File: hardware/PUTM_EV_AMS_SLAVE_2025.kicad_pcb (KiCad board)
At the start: 4 copper layers, 100 x 20 mm, 138 parts, among them CN7 4x100nF, IC2 BQ79616PAPR, J2 B02B-PASK-1, J3 B02B-PASK-1, J4 IDC24, Q2 100V/2W

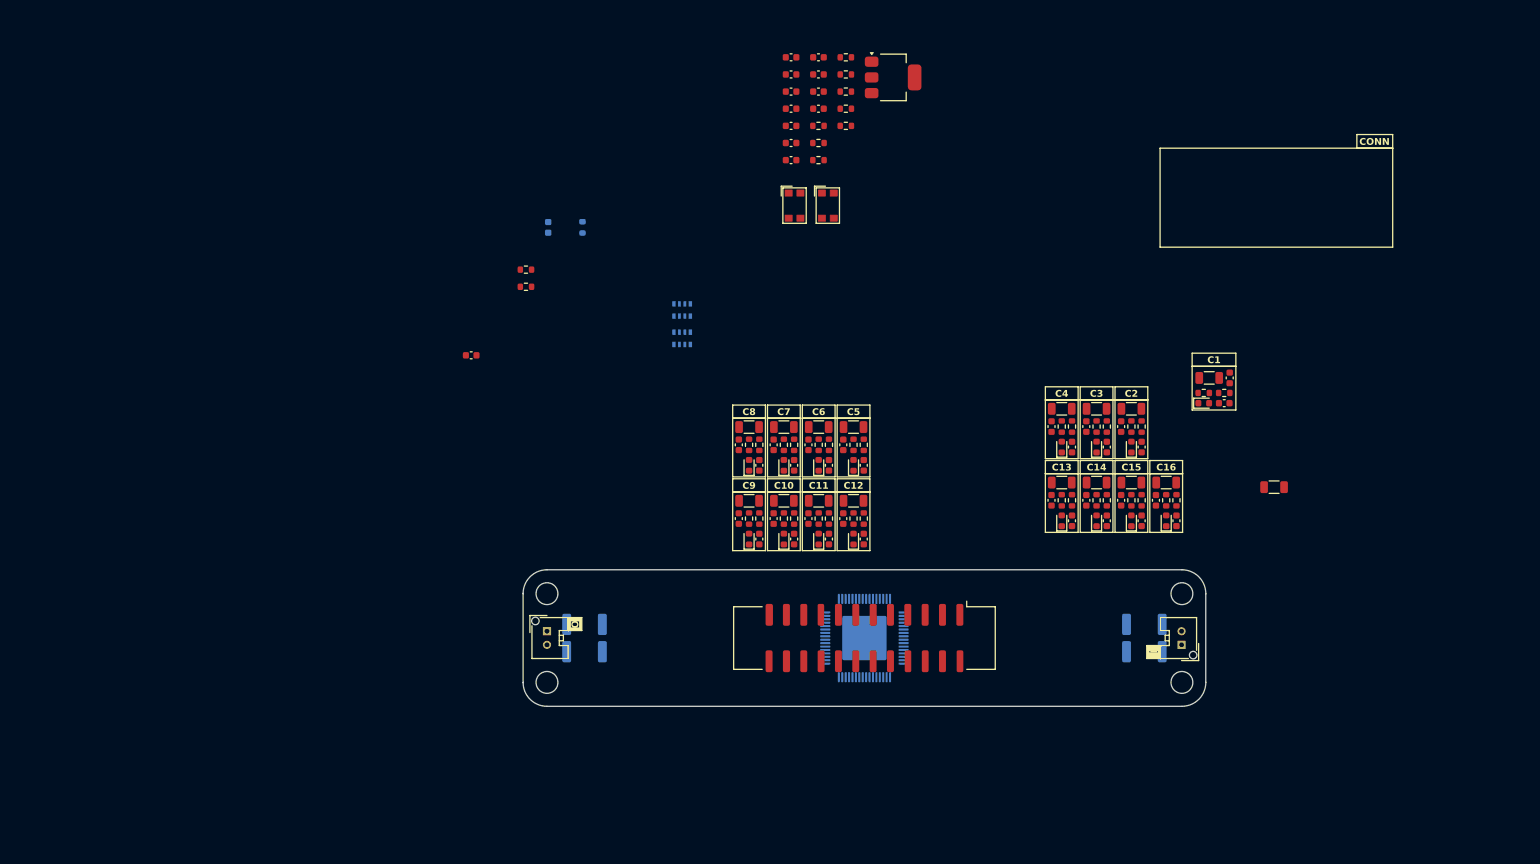
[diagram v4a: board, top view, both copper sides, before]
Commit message: changed back harwin connectors, COM first fitting
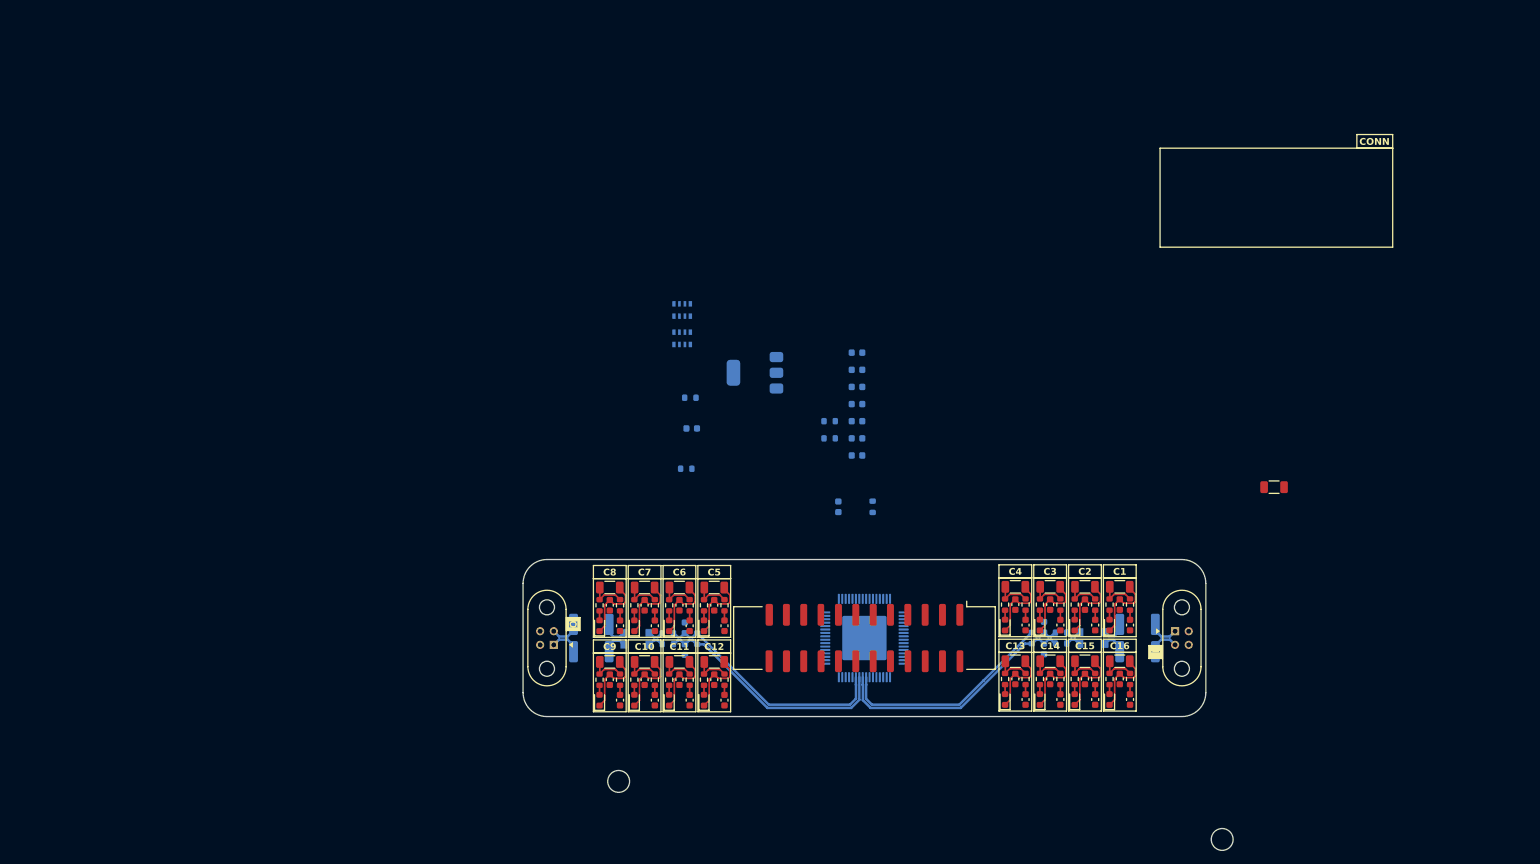
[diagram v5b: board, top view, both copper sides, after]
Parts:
- removed J3: B02B-PASK-1, Samacsys:B02BPASK1LFSN
- removed the REF** at (196.5, 113.5)
- removed the REF** at (103.5, 126.5)
- added J1: M80-5100405, Samacsys:M80-51004YY, F.Cu at (103.5, 120.0)
- C38, C39, C40, C41, C42, C43, C44, C45, C46, C47, C48, C49, L1, L2, Q2, R50, R52, R53, R54, R55, R56, R57, R58, R59, R60: moved to B.Cu
- J2: value B02B-PASK-1 -> M80-5100405; footprint Samacsys:B02BPASK1LFSN -> Samacsys:M80-51004YY
- moved J2 93.0 mm to (196.5, 120.0), turned to -90 degrees
- moved C47 90.4 mm to (176.3, 121.6), turned to -90 degrees
- moved C46 89.8 mm to (176.3, 118.4), turned to 90 degrees
- moved R56 88.3 mm to (121.2, 119.3)
- moved R57 87.4 mm to (121.2, 120.9), turned to 180 degrees
- moved R58 84.5 mm to (174.5, 120.0), turned to -90 degrees
- moved C48 84.0 mm to (123.7, 121.7), turned to -90 degrees
- moved R59 83.0 mm to (178.8, 119.2), turned to 180 degrees
- moved R60 82.1 mm to (178.8, 120.8)
- moved C49 78.5 mm to (123.7, 118.5), turned to 90 degrees
- moved L1 76.9 mm to (183.4, 120.0), turned to 90 degrees
- moved R55 72.3 mm to (125.5, 120.1), turned to 90 degrees
- moved L2 69.4 mm to (116.6, 120.1), turned to 90 degrees
- moved C4 59.0 mm to (146.2, 100.8)
- moved R2 59.0 mm to (151.2, 100.8)
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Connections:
- net /TH7+ renamed /AUX/TH7+
- net Net-(IC2-AVDD) renamed /BQ79616/AVDD
- net Net-(IC2-BAT) renamed /BQ79616/BAT
- net Net-(IC2-COMHN) renamed /BQ79616/IC_COMHN
- net Net-(IC2-COMHP) renamed /BQ79616/IC_COMHP
- net Net-(IC2-CVDD) renamed /BQ79616/CVDD
- net Net-(IC2-DVDD) renamed /BQ79616/DVDD
- net Net-(IC2-LDOIN) renamed /BQ79616/LDOIN
- net Net-(IC2-NEG5V) renamed /BQ79616/NEG5V
- net Net-(IC2-NPNB) renamed /BQ79616/NPNB
- net Net-(IC2-REFHP) renamed /BQ79616/REFHM
- net Net-(Q2-C) renamed /BQ79616/NPNC
- C46 pad 1: Net-(IC2-COMLN) -> /BQ79616/IC_COMLP
- C47 pad 1: Net-(IC2-COMLP) -> /BQ79616/IC_COMLN
- C5 pad 1: /IB+ -> /OL+
- C6 pad 1: /IB- -> /OL-
- C7 pad 1: /IN+ -> /IN-
- C7 pad 2: /IA+ -> /IL-
- C8 pad 1: /IN- -> /IN+
- C8 pad 2: /IA- -> /IL+
- IC2 pad 40: Net-(IC2-COMLP) -> /BQ79616/IC_COMLP
- IC2 pad 41: Net-(IC2-COMLN) -> /BQ79616/IC_COMLN
- J2 pad 1: Net-(J2-Pin_1) -> /IN+
- J2 pad 2: Net-(J2-Pin_2) -> /IN-
- L1 pad 1: Net-(J3-Pin_1) -> /IL-
- L1 pad 2: /IN+ -> /I-
- L1 pad 3: /IN- -> /I+
- L1 pad 4: Net-(J3-Pin_2) -> /IL+
- L2 pad 1: /OUT+ -> /O-
- L2 pad 2: Net-(J2-Pin_1) -> /OL-
- L2 pad 3: Net-(J2-Pin_2) -> /OL+
- L2 pad 4: /OUT- -> /O+
- R2 pad 2: Net-(RN7-R1.2) -> /BQ79616/TSREF
- R56 pad 1: /IB+ -> /O+
- R57 pad 2: /IB- -> /O-
- R58 pad 1: Net-(IC2-COMLN) -> /BQ79616/IC_COMLP
- R58 pad 2: Net-(IC2-COMLP) -> /BQ79616/IC_COMLN
- R59 pad 1: /IA- -> /I+
- R59 pad 2: Net-(IC2-COMLN) -> /BQ79616/IC_COMLP
- R60 pad 1: Net-(IC2-COMLP) -> /BQ79616/IC_COMLN
- R60 pad 2: /IA+ -> /I-
- RN7 pad 5: Net-(RN7-R1.2) -> /BQ79616/TSREF
- RN7 pad 6: Net-(RN7-R1.2) -> /BQ79616/TSREF
- RN7 pad 7: Net-(RN7-R1.2) -> /BQ79616/TSREF
- RN7 pad 8: Net-(RN7-R1.2) -> /BQ79616/TSREF
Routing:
- net /BQ79616/IC_COMLN: track 0.00 -> 36.9 mm
- net /BQ79616/IC_COMLP: track 0.00 -> 36.6 mm
- net /BQ79616/IC_COMHN: track 0.00 -> 35.9 mm
- net /BQ79616/IC_COMHP: track 0.00 -> 35.6 mm
- net /BQ79616/CB5: track 0.00 -> 10.7 mm
- net /BQ79616/CB4: track 0.00 -> 10.7 mm
- net /BQ79616/CB3: track 0.00 -> 10.7 mm
- net /BQ79616/CB12: track 0.00 -> 10.7 mm
- net /BQ79616/CB7: track 0.00 -> 10.7 mm
- net /BQ79616/CB6: track 0.00 -> 10.7 mm
- net /BQ79616/CB8: track 0.00 -> 10.7 mm
- net /BQ79616/CB13: track 0.00 -> 10.7 mm
- net /BQ79616/CB14: track 0.00 -> 10.7 mm
- net /BQ79616/CB10: track 0.00 -> 10.7 mm
- net /BQ79616/CB11: track 0.00 -> 10.7 mm
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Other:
- board size 100 x 20 mm -> 100 x 23 mm

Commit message: sync
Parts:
- moved R51 44.1 mm to (166.8, 106.7)
- moved REF** 30.8 mm to (103.5, 112.0)
- moved REF** 22.2 mm to (196.5, 128.1)
- moved J2 3.80 mm to (196.5, 116.2)
- moved J1 3.70 mm to (103.5, 123.7)
- moved C48 2.70 mm to (126.4, 121.7)
- moved C49 2.70 mm to (126.4, 118.5)
- moved C5 2.70 mm to (112.7, 118.0)
- moved C6 2.70 mm to (112.7, 122.0)
- moved L2 2.70 mm to (119.3, 120.1)
- moved R56 2.70 mm to (123.9, 119.3)
- moved R57 2.70 mm to (123.9, 120.9)
- moved R55 2.70 mm to (128.2, 120.1)
- moved C46 2.60 mm to (173.7, 118.4)
- moved C47 2.60 mm to (173.7, 121.6)
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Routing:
- net /BQ79616/IC_COMLN: track 36.9 -> 0.00 mm
- net /BQ79616/IC_COMLP: track 36.6 -> 0.00 mm
- net /BQ79616/IC_COMHN: track 35.9 -> 0.00 mm
- net /BQ79616/IC_COMHP: track 35.6 -> 0.00 mm
- net /OL+: track 4.80 -> 0.00 mm
- net /OUT-: track 4.47 -> 0.00 mm
- net /OUT+: track 4.47 -> 0.00 mm
- net /IN-: track 4.47 -> 0.00 mm
- net /IN+: track 4.47 -> 0.00 mm
- net /OL-: track 3.64 -> 0.00 mm
- net /IL+: track 3.62 -> 0.00 mm
- net /IL-: track 3.56 -> 0.00 mm
- net /O-: track 2.52 -> 0.00 mm
- net /O+: track 2.52 -> 0.00 mm
- net /I-: track 2.43 -> 0.00 mm
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
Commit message: some visual touch ups, added aux diodes for checking comm with IC, temp meas section, fliped the connector to the other side etc.
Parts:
- removed C4: 100nF, Capacitor_SMD:C_0603_1608Metric
- removed CN7: 4x100nF, Resistor_SMD:R_Array_Convex_4x0603
- added D17: LED, LED_SMD:LED_0603_1608Metric, F.Cu at (153.2, 95.0)
- added D18: LED, LED_SMD:LED_0603_1608Metric, F.Cu at (153.2, 97.5)
- added R61: 510, Resistor_SMD:R_0603_1608Metric, F.Cu at (149.7, 95.0)
- added RN1: 4x10k, Resistor_SMD:R_Array_Convex_4x0603, F.Cu at (163.5, 117.5)
- added TH1: 10k/β=?, Resistor_SMD:R_0603_1608Metric, F.Cu at (149.7, 97.5)
- added TH2: 10k/β=?, Resistor_SMD:R_0603_1608Metric, F.Cu at (149.7, 100.0)
- C38, C40, C41, C42, C43, C44, C45, IC2, Q2, R50, R53, R54, RN7: moved to F.Cu
- C39: value 10nF -> 10nF/100V; moved to F.Cu
- J4: moved to B.Cu
- R2: value 10k -> 510; moved to F.Cu
- R52: value 30 -> 30/100mW; moved to F.Cu
- moved R52 61.4 mm to (184.7, 104.0), turned to 0 degrees
- moved C38 61.3 mm to (184.7, 102.0), turned to 0 degrees
- moved RN7 60.6 mm to (163.5, 121.5), turned to 0 degrees
- moved R53 49.3 mm to (193.3, 98.0), turned to 0 degrees
- moved R54 49.3 mm to (193.3, 100.5), turned to 0 degrees
- moved Q2 45.5 mm to (178.5, 90.5), turned to 0 degrees
- moved C39 41.5 mm to (189.3, 88.0), turned to 0 degrees
- moved R50 34.2 mm to (157.2, 95.0), turned to 0 degrees
- moved C40 13.7 mm to (161.7, 85.5), turned to 0 degrees
- moved C43 13.7 mm to (161.7, 93.0), turned to 0 degrees
- moved C41 13.7 mm to (161.7, 88.0), turned to 0 degrees
- moved C42 13.7 mm to (161.7, 90.5), turned to 0 degrees
- moved C44 13.7 mm to (161.7, 95.5), turned to 0 degrees
- moved C45 13.7 mm to (161.7, 98.1), turned to 0 degrees
- moved R2 9.78 mm to (151.5, 91.0), turned to 0 degrees
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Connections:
- C38 pad 1: /BQ79616/C1- -> /C1-
- C39 pad 2: /BQ79616/C1- -> /C1-
- C40 pad 2: /BQ79616/C1- -> /C1-
- C41 pad 2: /BQ79616/C1- -> /C1-
- C42 pad 2: /BQ79616/C1- -> /C1-
- C43 pad 2: /BQ79616/C1- -> /C1-
- C44 pad 2: /BQ79616/C1- -> /C1-
- C45 pad 2: /BQ79616/C1- -> /C1-
- C46 pad 2: /BQ79616/C1- -> /C1-
- C47 pad 2: /BQ79616/C1- -> /C1-
- C48 pad 2: /BQ79616/C1- -> /C1-
- C49 pad 2: /BQ79616/C1- -> /C1-
- IC2 pad 36: /BQ79616/C1- -> /C1-
- IC2 pad 39: /BQ79616/C1- -> /C1-
- IC2 pad 46: /BQ79616/C1- -> /C1-
- IC2 pad 50: /BQ79616/C1- -> /C1-
- IC2 pad 54: unconnected-(IC2-GPIO8-Pad54) -> /BQ79616/AUX2/TH8+
- IC2 pad 55: unconnected-(IC2-GPIO7-Pad55) -> /AUX/TH7+
- IC2 pad 56: unconnected-(IC2-GPIO6-Pad56) -> /TH6+
- IC2 pad 57: unconnected-(IC2-GPIO5-Pad57) -> /TH5+
- IC2 pad 58: unconnected-(IC2-GPIO4-Pad58) -> /TH4+
- IC2 pad 59: unconnected-(IC2-GPIO3-Pad59) -> /TH3+
- IC2 pad 60: unconnected-(IC2-GPIO2-Pad60) -> /TH2+
- IC2 pad 61: unconnected-(IC2-GPIO1-Pad61) -> /TH1+
- IC2 pad 65: /BQ79616/C1- -> /C1-
- R2 pad 1: /TH1+ -> /BQ79616/CVDD
- R2 pad 2: /BQ79616/TSREF -> Net-(D17-A)
- R50 pad 1: /BQ79616/C1- -> /C1-
- R51 pad 1: /BQ79616/C1- -> /C1-
- R54 pad 1: /BQ79616/C1- -> /C1-
- RN7 pad 1: /TH2+ -> /TH5+
- RN7 pad 2: /TH3+ -> /TH6+
- RN7 pad 3: /TH4+ -> /AUX/TH7+
- RN7 pad 4: /TH5+ -> /BQ79616/AUX2/TH8+
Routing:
- net /OUT-: track 0.00 -> 6.84 mm
- net /OUT+: track 0.00 -> 6.84 mm
- net /IN-: track 0.00 -> 6.54 mm
- net /IN+: track 0.00 -> 6.54 mm
- net /BQ79616/IC_COMHP: track 0.00 -> 4.44 mm
- net /BQ79616/IC_COMHN: track 0.00 -> 4.44 mm
- net /BQ79616/IC_COMLP: track 0.00 -> 4.44 mm
- net /BQ79616/IC_COMLN: track 0.00 -> 4.44 mm
- net /IL-: track 0.00 -> 2.62 mm
- net /IL+: track 0.00 -> 2.62 mm
- net /OL-: track 0.00 -> 2.62 mm
- net /OL+: track 0.00 -> 2.62 mm
- net /O-: track 0.00 -> 2.43 mm
- net /O+: track 0.00 -> 2.43 mm
- net /I-: track 0.00 -> 2.43 mm
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
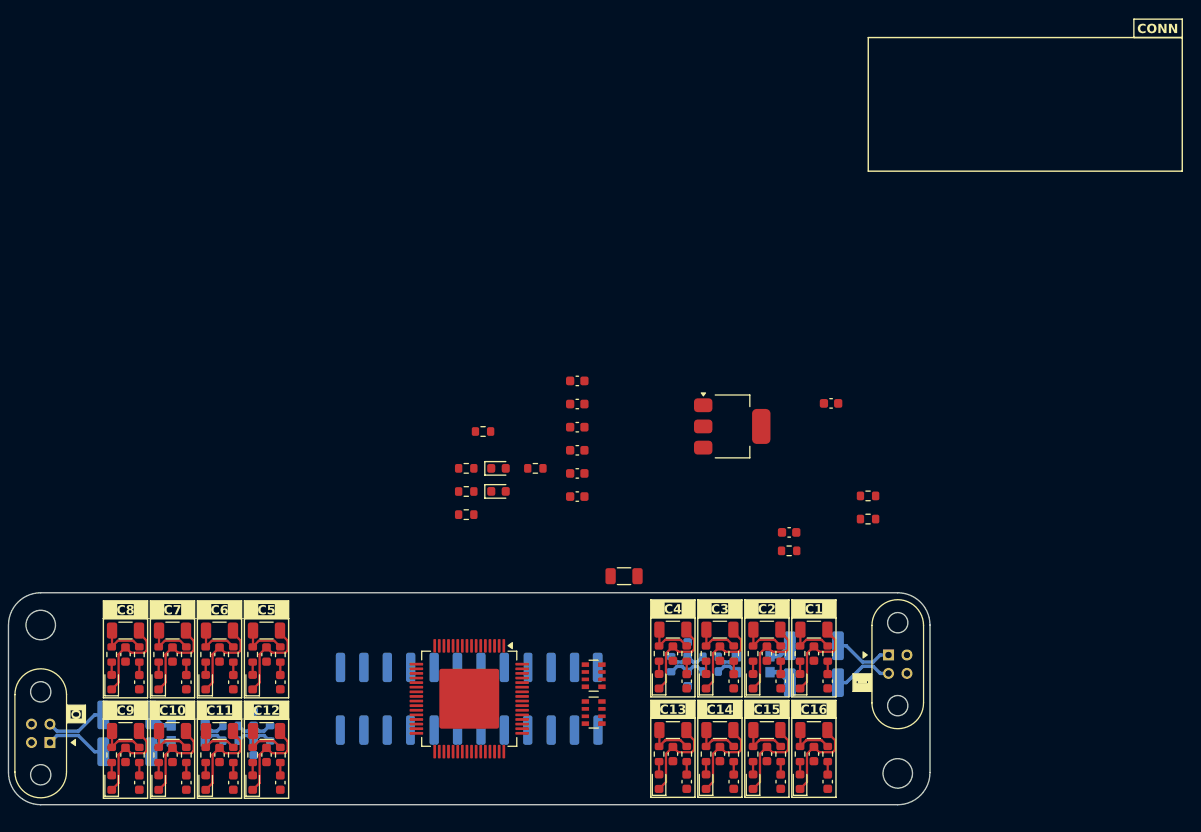
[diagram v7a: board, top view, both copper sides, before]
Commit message: pcb layout 99.9% done - all sections named and placed also some initial routing
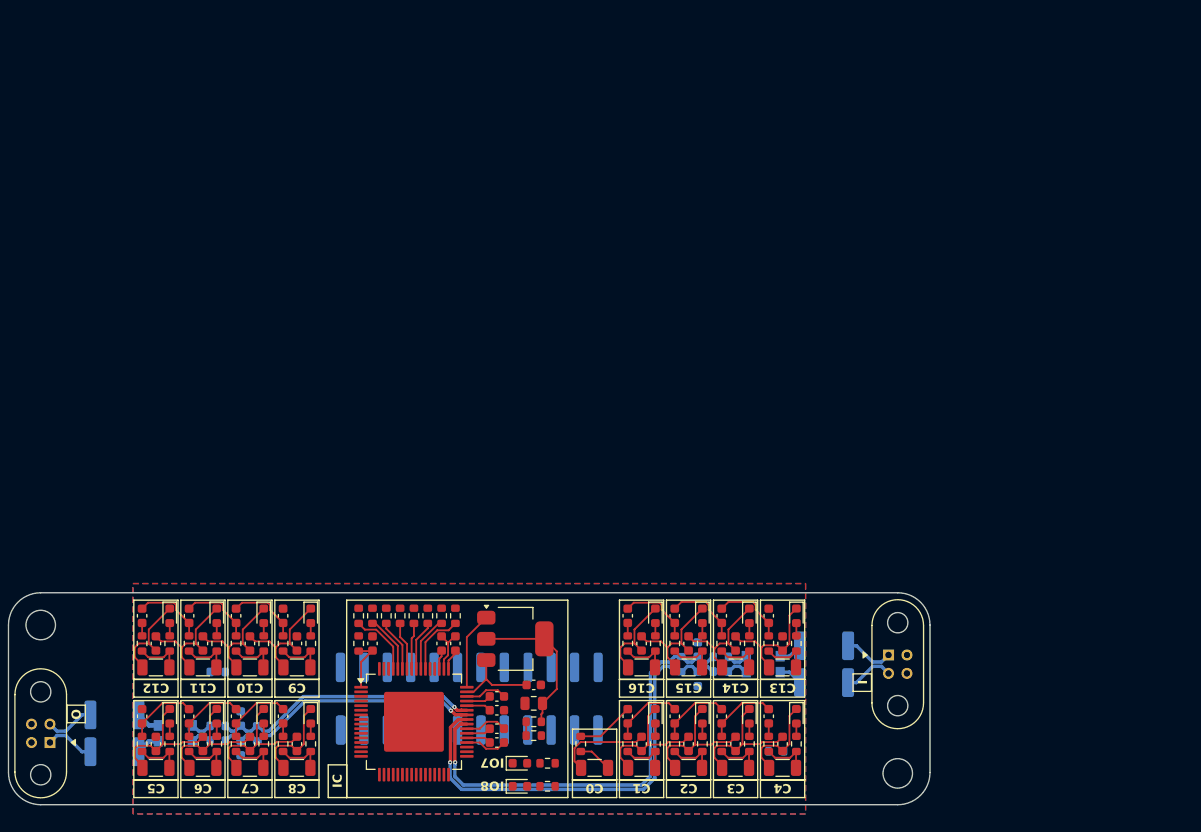
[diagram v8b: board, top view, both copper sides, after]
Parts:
- removed RN1, RN7: 4x10k, Resistor_SMD:R_Array_Convex_4x0603
- added C4: 100nF, Capacitor_SMD:C_0603_1608Metric, F.Cu at (157.0, 118.5)
- added R62: 10k, Resistor_SMD:R_0603_1608Metric, F.Cu at (138.0, 111.0)
- added R63: 10k, Resistor_SMD:R_0603_1608Metric, F.Cu at (139.5, 111.0)
- added R64: 10k, Resistor_SMD:R_0603_1608Metric, F.Cu at (141.0, 111.0)
- added R65: 10k, Resistor_SMD:R_0603_1608Metric, F.Cu at (142.5, 111.0)
- added R66: 10k, Resistor_SMD:R_0603_1608Metric, F.Cu at (144.0, 111.0)
- added R67: 10k, Resistor_SMD:R_0603_1608Metric, F.Cu at (145.5, 111.0)
- added R68: 10k, Resistor_SMD:R_0603_1608Metric, F.Cu at (147.0, 111.0)
- added R69: 10k, Resistor_SMD:R_0603_1608Metric, F.Cu at (148.5, 111.0)
- C39: value 10nF/100V -> 220nF/100V; footprint Capacitor_SMD:C_0603_1608Metric -> Capacitor_SMD:C_0805_2012Metric
- TH1, TH2: moved to B.Cu
- moved R52 47.8 mm to (138.0, 114.0), turned to -90 degrees
- moved C38 46.8 mm to (139.5, 114.0), turned to -90 degrees
- moved C39 45.8 mm to (157.0, 120.5), turned to 180 degrees
- moved R53 43.8 mm to (157.0, 122.5)
- moved R54 43.2 mm to (157.0, 124.0), turned to 180 degrees
- moved TH2 42.3 mm to (183.3, 125.7)
- moved C40 38.7 mm to (153.0, 123.2)
- moved R2 36.7 mm to (158.5, 127.0), turned to 180 degrees
- moved R61 35.6 mm to (158.5, 129.5), turned to 180 degrees
- moved C41 34.4 mm to (153.0, 121.2)
- moved TH1 33.3 mm to (122.7, 117.1), turned to 180 degrees
- moved Q2 32.9 mm to (155.0, 113.5)
- moved C43 32.9 mm to (153.0, 124.8)
- moved D17 32.1 mm to (155.5, 127.0)
- moved D18 32.1 mm to (155.5, 129.5)
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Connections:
- net /BQ79616/IC_COMHN renamed /OIC-
- net /BQ79616/IC_COMHP renamed /OIC+
- net /BQ79616/IC_COMLN renamed /IIC-
- net /BQ79616/IC_COMLP renamed /IIC+
- net /I+ renamed /ILR+
- net /I- renamed /ILR-
- net /IL+ renamed /ILC+
- net /IL- renamed /ILC-
- net /IN+ renamed /ICC+
- net /IN- renamed /ICC-
- net /O+ renamed /ORL+
- net /O- renamed /ORL-
- net /OL+ renamed /OLC+
- net /OL- renamed /OLC-
- net /OUT+ renamed /OCC+
- net /OUT- renamed /OCC-
- C38 pad 1: /C1- -> GND
- C39 pad 2: /C1- -> GND
- C40 pad 2: /C1- -> GND
- C41 pad 2: /C1- -> GND
- C42 pad 2: /C1- -> GND
- C43 pad 2: /C1- -> GND
- C44 pad 2: /C1- -> GND
- C45 pad 2: /C1- -> GND
- C46 pad 2: /C1- -> GND
- C47 pad 2: /C1- -> GND
- C48 pad 2: /C1- -> GND
- C49 pad 2: /C1- -> GND
- IC2 pad 36: /C1- -> GND
- IC2 pad 39: /C1- -> GND
- IC2 pad 46: /C1- -> GND
- IC2 pad 50: /C1- -> GND
- IC2 pad 63: /C8+ -> unconnected-(IC2-BBN-Pad63)
- IC2 pad 64: /C9+ -> unconnected-(IC2-BBP-Pad64)
- IC2 pad 65: /C1- -> GND
- J4 pad 1: /C1- -> GND
- R50 pad 1: /C1- -> GND
- R51 pad 1: /C1- -> GND
- R54 pad 1: /C1- -> /C16+
- TH1 pad 2: /C1- -> GND
- TH2 pad 2: /C1- -> GND
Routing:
- net /IIC-: track 4.44 -> 50.0 mm, vias 0 -> 1
- net /IIC+: track 4.44 -> 48.4 mm, vias 0 -> 1
- net /OIC-: track 4.44 -> 29.6 mm, vias 0 -> 1
- net /OIC+: track 4.44 -> 29.6 mm, vias 0 -> 1
- net GND: track 0.00 -> 22.7 mm
- net /BQ79616/NPNC: track 0.00 -> 16.6 mm
- net /BQ79616/CB0: track 0.00 -> 10.2 mm
- net /BQ79616/LDOIN: track 0.00 -> 9.39 mm
- net /BQ79616/NPNB: track 0.00 -> 8.42 mm
- net /TH1+: track 0.00 -> 7.21 mm
- net /BQ79616/AUX2/TH8+: track 0.00 -> 7.00 mm
- net /BQ79616/VC13: track 1.47 -> 8.13 mm
- net /BQ79616/VC14: track 1.47 -> 8.13 mm
- net /BQ79616/VC11: track 1.47 -> 8.07 mm
- net /BQ79616/VC10: track 1.47 -> 8.07 mm
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- added copper zone on B.Cu, net GND
- added copper zone on F.Cu, net GND
- added copper zone on In1.Cu, net GND
- added copper zone on In2.Cu, net GND
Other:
- board text added: "C0"
- board text added: "IC"
- board text added: "IO7"
- board text added: "IO8"
